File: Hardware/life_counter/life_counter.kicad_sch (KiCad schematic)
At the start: 22 parts, among them J1 XIAO_BAT_LINK, P1 OLED-DISPLAY, Q1 Q-PMOS, U1 XIAO ESP32C3

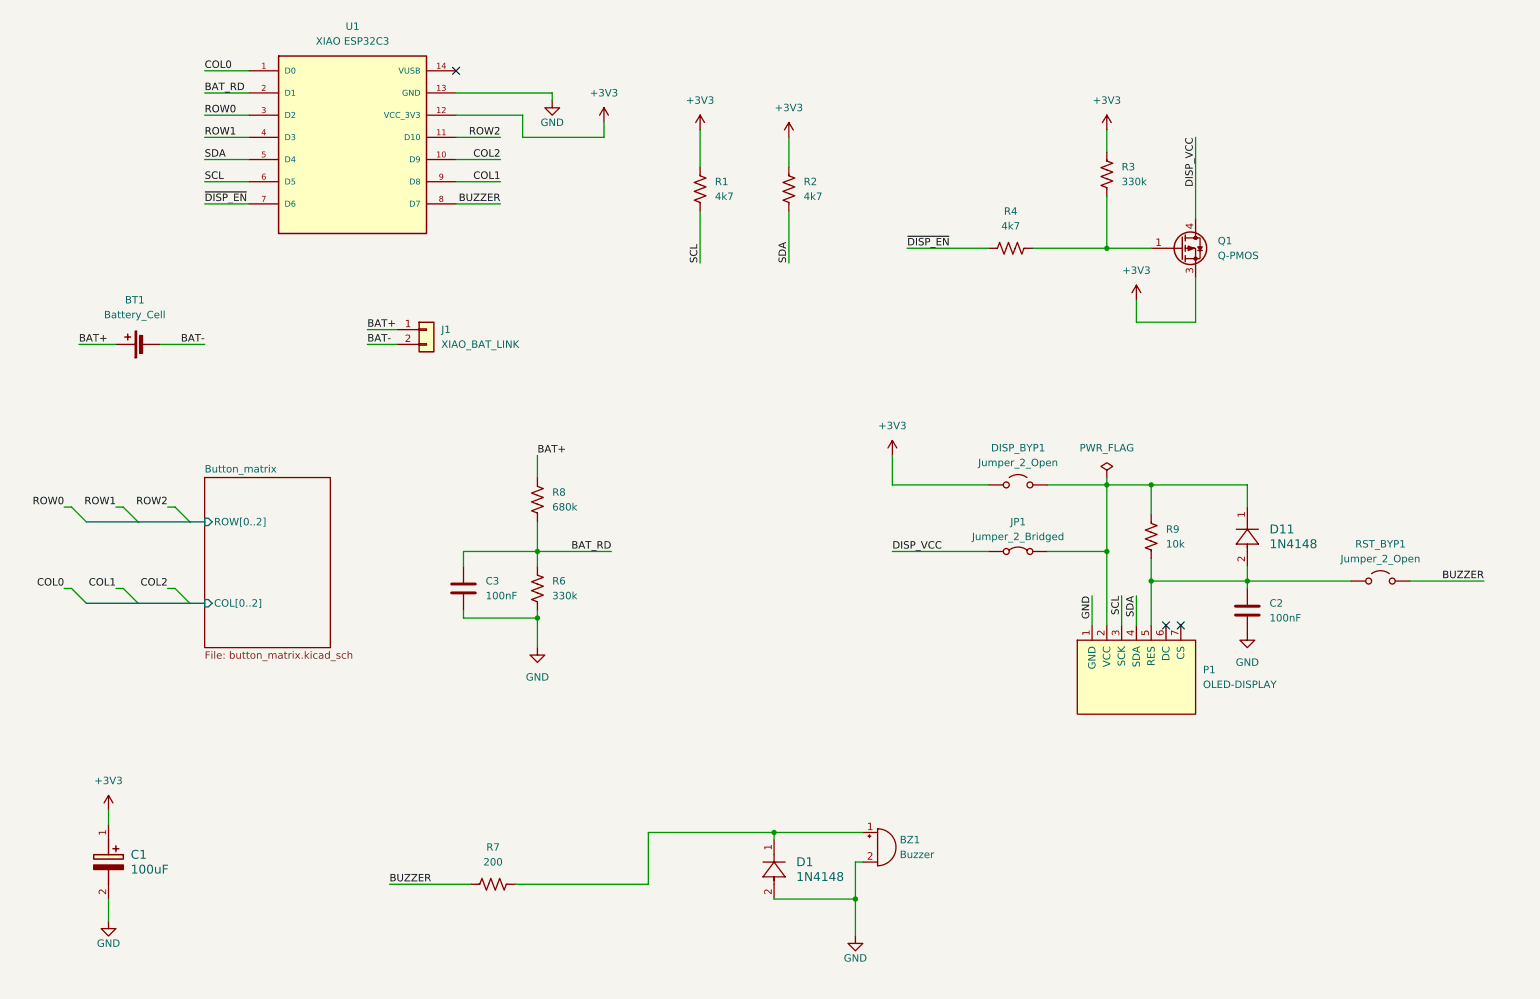
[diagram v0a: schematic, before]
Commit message: updated the kicad schematics, added auto shut off when battery is at 3.3V, added an image folder forthe  github page
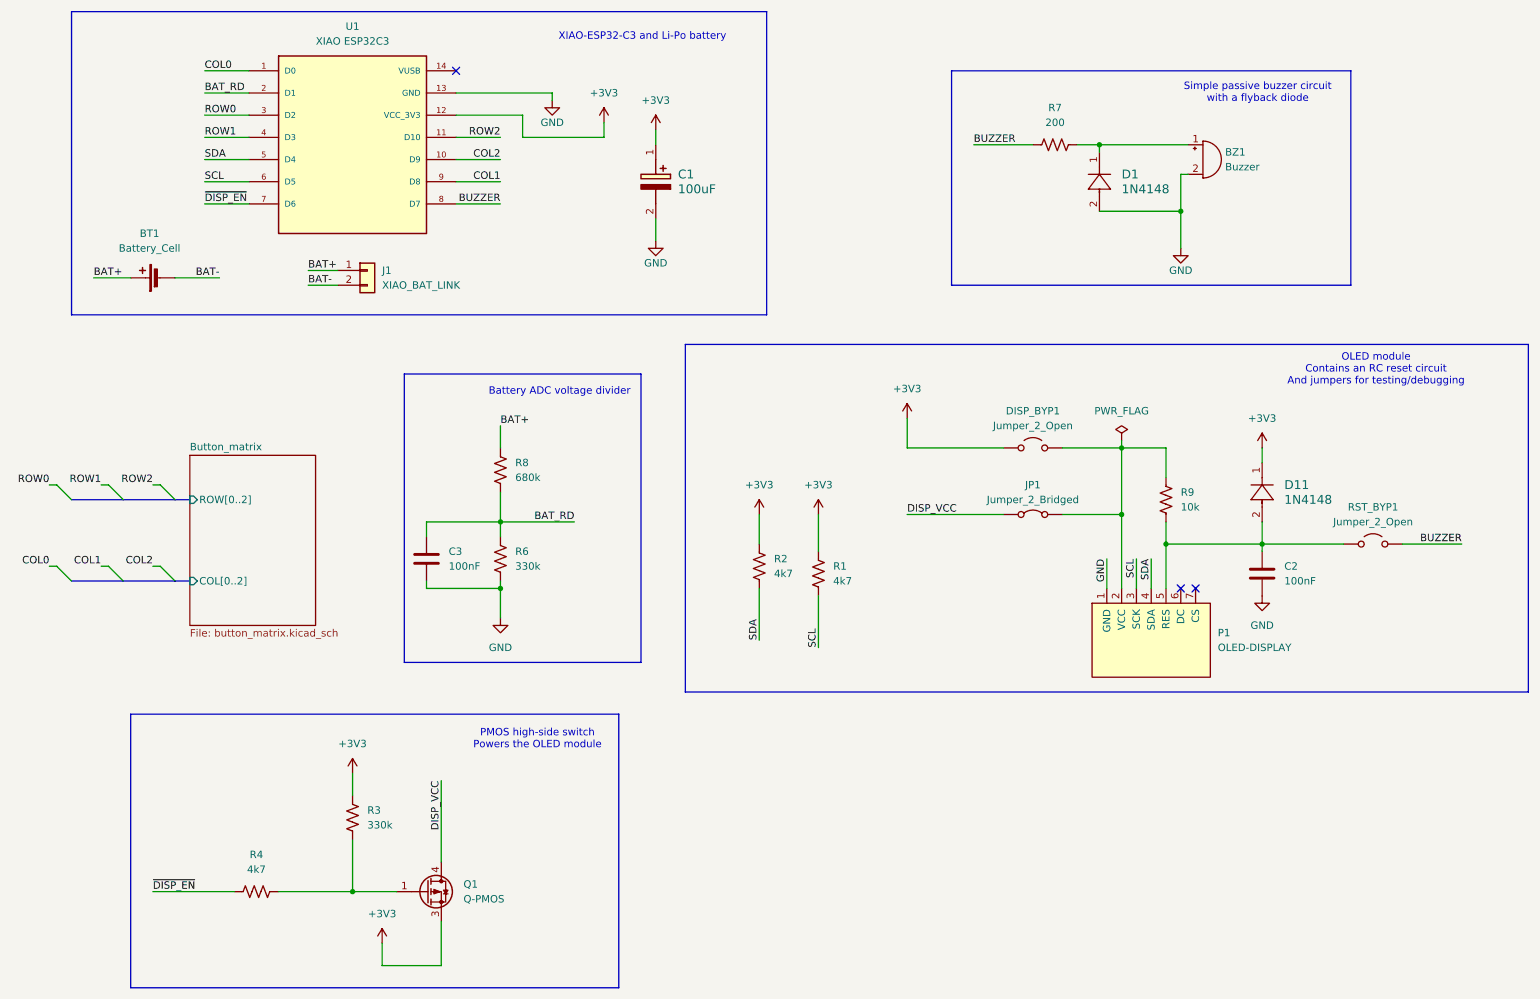
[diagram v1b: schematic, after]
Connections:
- net +3V3: now also D11.1
- net at DISP_BYP1.2 (B), JP1.2 (B), P1.2 (VCC)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: no longer D11.1
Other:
- note added: "Battery ADC voltage divider"
- note added: "OLED module Contains an RC reset circuit And jumpers for testing/debugging"
- note added: "PMOS high-side switch Powers the OLED module"
- note added: "Simple passive buzzer circuit with a flyback diode"
- note added: "XIAO-ESP32-C3 and Li-Po battery"
- company: (none) -> Emilia Kozioł
- title: (none) -> TcgLifeCounter
- moved on the sheet: BT1, BZ1, C1, C2, C3, D1, D11, DISP_BYP1, J1, JP1, P1, Q1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
